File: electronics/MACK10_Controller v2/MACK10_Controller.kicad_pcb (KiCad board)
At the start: 2 copper layers, 57.3 x 67.1 mm, 60 parts, among them J10 BYP_2, J2 Motor, J3 J_Expansion, J4 I/O, J5 Sensor IDC, J6 Interface IDC, J7 Fan, J8 E_STOP, J9 24V IN, Q1 SS8550, U1 TMC2208, U2 HX711, U3 XIAO-C6, U4 INA226, U5 PCF8575, U6 MINI360

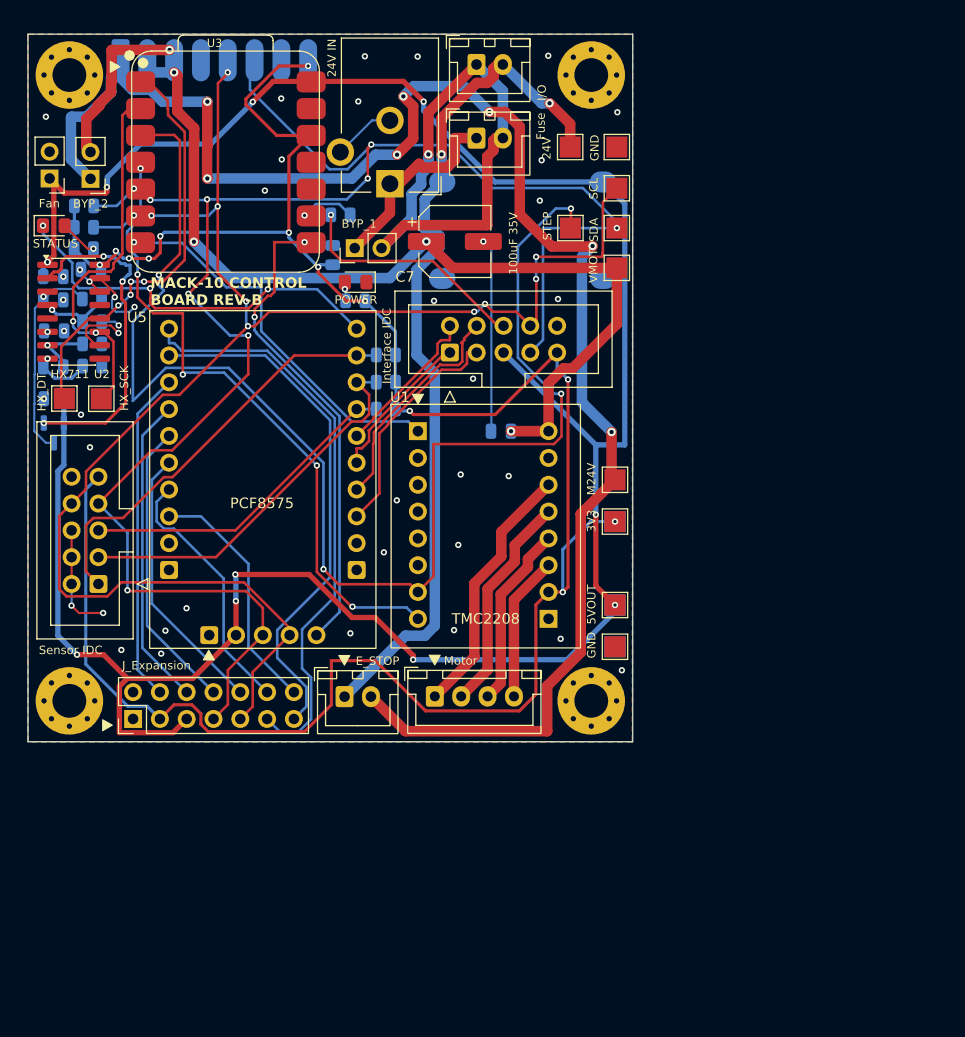
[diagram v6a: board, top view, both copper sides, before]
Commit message: Resolved DRC warnings, fixed thermal reliefs and clearance issues, rerouted some traces.
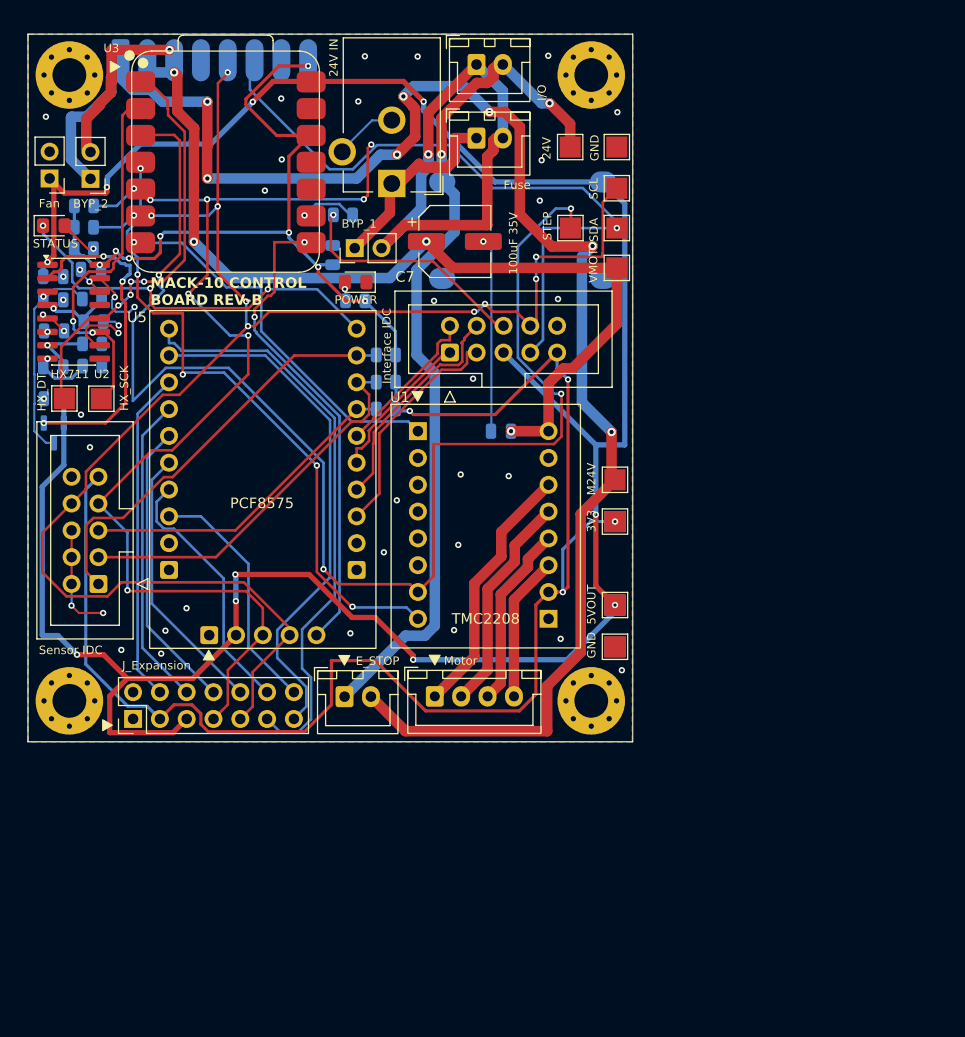
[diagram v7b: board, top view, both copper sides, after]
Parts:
- moved R5 0.24 mm to (47.1, 34.4)
- moved J9 0.18 mm to (51.7, 31.4)
- moved R4 0.12 mm to (23.4, 44.5)
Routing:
- net /+5V: track 232.6 -> 235.9 mm, vias 11 -> 10
- net /GND: track 34.8 -> 37.5 mm
- net /SCL: track 154.5 -> 155.8 mm, vias 12 -> 10
- net /SDA: track 170.0 -> 170.9 mm, vias 10 -> 9
- net /+24V: track 82.1 -> 81.4 mm
- net /3V3: vias 13 -> 12
- net Net-(F1-Pin_2): vias 2 -> 1

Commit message: Added EN for reboot, finishing touches
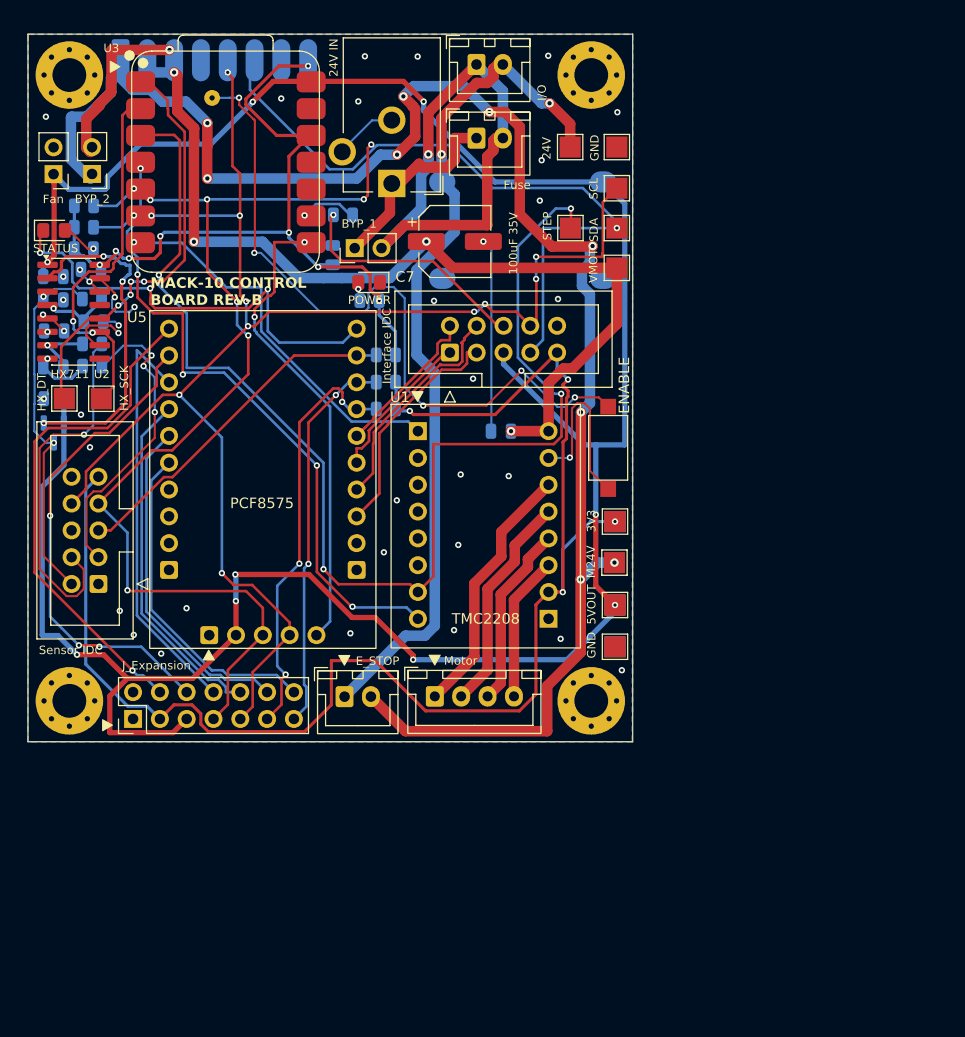
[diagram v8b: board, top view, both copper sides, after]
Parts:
- added SW1: ENABLE, Button_Switch_SMD:SW_SPST_CK_RS282G05A3, F.Cu at (72.2, 56.5)
- moved TP7 7.85 mm to (72.8, 67.3)
- moved R6 1.35 mm to (49.6, 42.5)
- moved D1 1.28 mm to (49.5, 40.8)
- moved J7 0.56 mm to (19.6, 30.5)
- moved J10 0.48 mm to (23.3, 30.5)
- moved D2 0.45 mm to (19.7, 35.9)
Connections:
- C3 pad 1: Net-(J1-Shield) -> /E+
- J3 pad 10: /IO6 -> /IO4
- J3 pad 11: /IO1 -> /LIM_TOP
- J3 pad 12: /IO7 -> /IO5
- J3 pad 13: /IO2 -> /LIM_BOT
- J3 pad 14: /IO8 -> /IO6
- J3 pad 4: /IO3 -> /IO1
- J3 pad 6: /IO4 -> /IO2
- J3 pad 8: /IO5 -> /IO3
- J5 pad 1: /E_STOP_SENSE -> /GND
- J5 pad 2: /GND -> /E+
- J5 pad 3: /LIM_BOT -> /A+
- J5 pad 4: /GND -> /A-
- J5 pad 5: /LIM_TOP -> /E_STOP_SENSE
- Q1 pad 3: Net-(J1-Shield) -> /E+
- R1 pad 1: Net-(J1-A-) -> /A-
- R2 pad 1: Net-(J1-E-) -> /A+
- R3 pad 2: Net-(J1-Shield) -> /E+
- U2 pad 3: Net-(J1-Shield) -> /E+
- U5 pad 22: /IO7 -> unconnected-(U5-P16-Pad22)
- U5 pad 23: /IO8 -> unconnected-(U5-P17-Pad23)
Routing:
- net Net-(U3-EN): track 0.00 -> 68.6 mm, vias 0 -> 6
- net /E+: track 0.00 -> 35.1 mm, vias 0 -> 2
- net /A-: track 0.00 -> 34.6 mm, vias 0 -> 1
- net /A+: track 0.00 -> 29.5 mm, vias 0 -> 3
- net /IO7: track 24.6 -> 0.00 mm
- net /IO8: track 23.3 -> 0.00 mm
- net Net-(J1-Shield): track 20.3 -> 0.00 mm, vias 1 -> 0
- net /STEP: track 130.1 -> 120.2 mm
- net /LIM_TOP: track 31.1 -> 40.1 mm, vias 0 -> 3
- net /IO3: track 31.5 -> 39.7 mm
- net /IO1: track 55.3 -> 48.3 mm, vias 0 -> 1
- net /E_STOP_SENSE: track 40.2 -> 33.2 mm
- net /GND: track 37.5 -> 44.3 mm, vias 42 -> 39
- net /SCL: track 155.8 -> 149.9 mm, vias 10 -> 12
- net /IO6: track 25.9 -> 31.4 mm
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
